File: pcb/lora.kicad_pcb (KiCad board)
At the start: 4 copper layers, 101.9 x 45.1 mm, 91 parts, among them J1 Conn_01x04, J11 Conn_Coaxial, J2 5V, J3 Conn_01x06, J4 USB_C_Receptacle_USB2.0, J5 Temp, J6 VDD, J7 UART, J8 Conn_01x04, Q1 AO3401A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

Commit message: changed a capacity
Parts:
- C3: value 47u -> 10u; footprint Capacitor_SMD:C_1210_3225Metric -> Capacitor_SMD:C_0805_2012Metric
- C4: value 47u -> 22u
- moved R3 3.89 mm to (222.2, 130.3), turned to -90 degrees
- moved SW1 3.56 mm to (225.8, 132.6)
- moved C3 0.62 mm to (185.2, 103.4)
- renumbered Ce to C13
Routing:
- net RESET: track 35.5 -> 31.3 mm
- net GND: track 235.0 -> 230.8 mm
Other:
- outline, holes or cut-outs redrawn
- board text added: "+"
- board text added: "Active"
- board text removed: "Status"

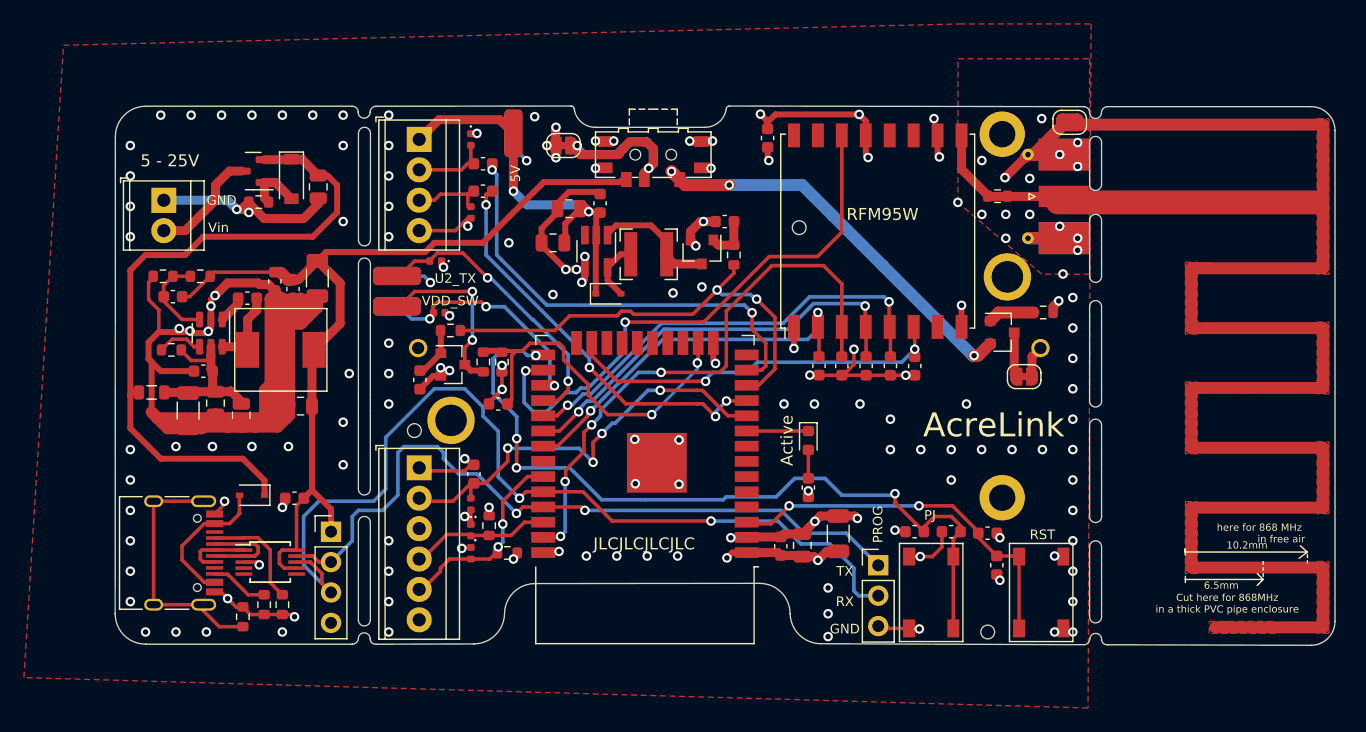
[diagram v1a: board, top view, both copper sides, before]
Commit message: added cutout for cable tie to secure battery
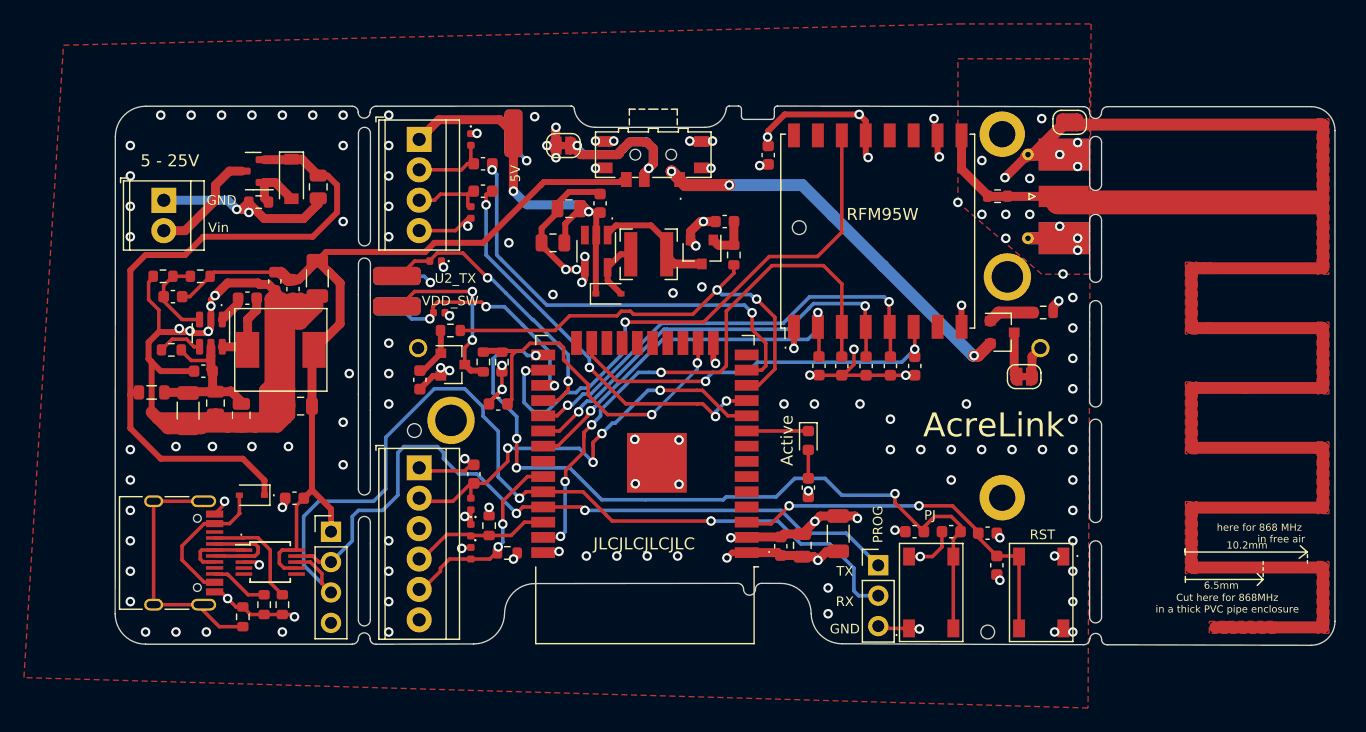
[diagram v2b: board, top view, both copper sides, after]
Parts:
- moved C9 1.43 mm to (203.1, 96.0)
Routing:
- net VDD: track 57.1 -> 56.6 mm
- net GND: track 230.8 -> 230.4 mm, vias 145 -> 144
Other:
- outline, holes or cut-outs redrawn
- board text added: "."

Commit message: updated readme
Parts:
- R1, R11, R13, R17, R2, R20, R23, R24, R3, R4, R5, R6, R9: footprint Capacitor_SMD:C_0603_1608Metric -> Resistor_SMD:R_0603_1608Metric
- moved JP3 1.08 mm to (185.1, 95.8)
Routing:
- net Net-(JP3-Pad1): track 20.6 -> 11.0 mm
- net VDD: track 56.6 -> 55.6 mm
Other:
- board text added: "V_EXT"
- board text removed: "V_EXT/OFF"

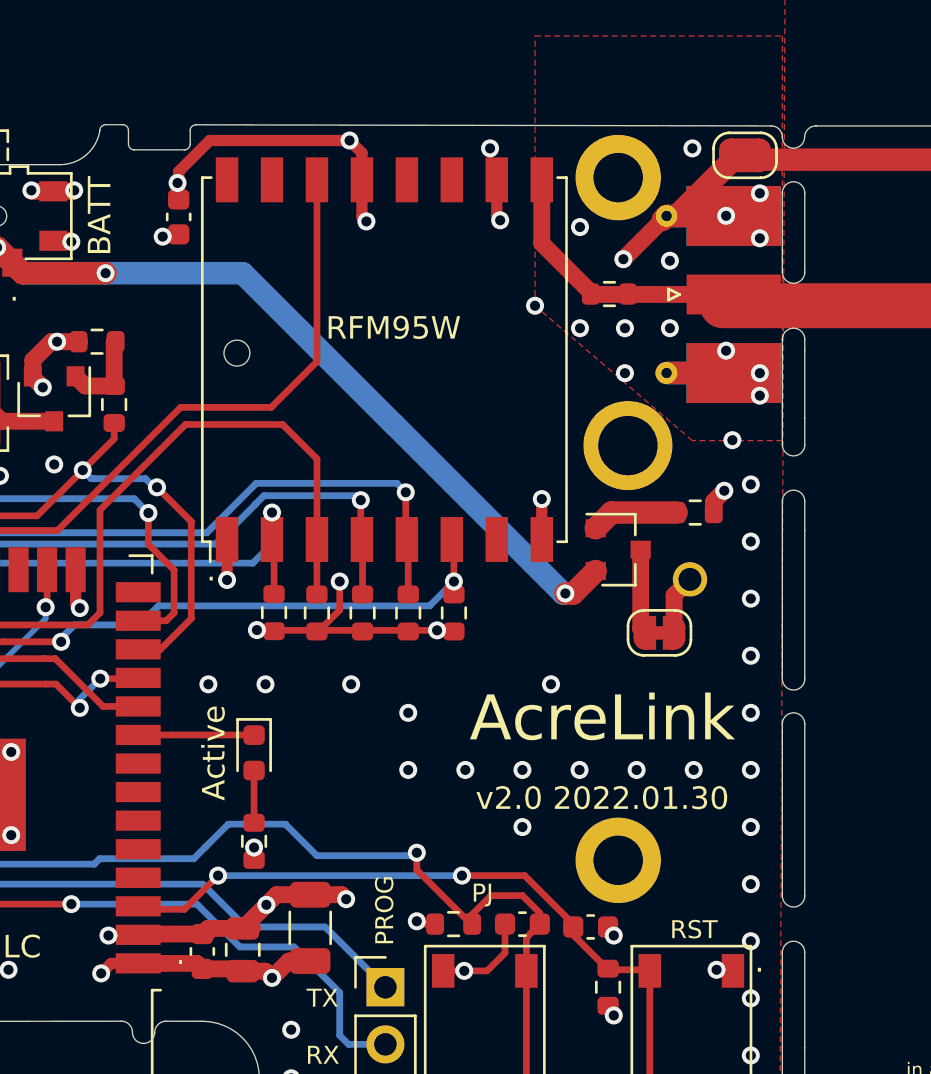
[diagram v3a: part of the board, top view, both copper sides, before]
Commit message: added spi header and connected dio1 of rfm95
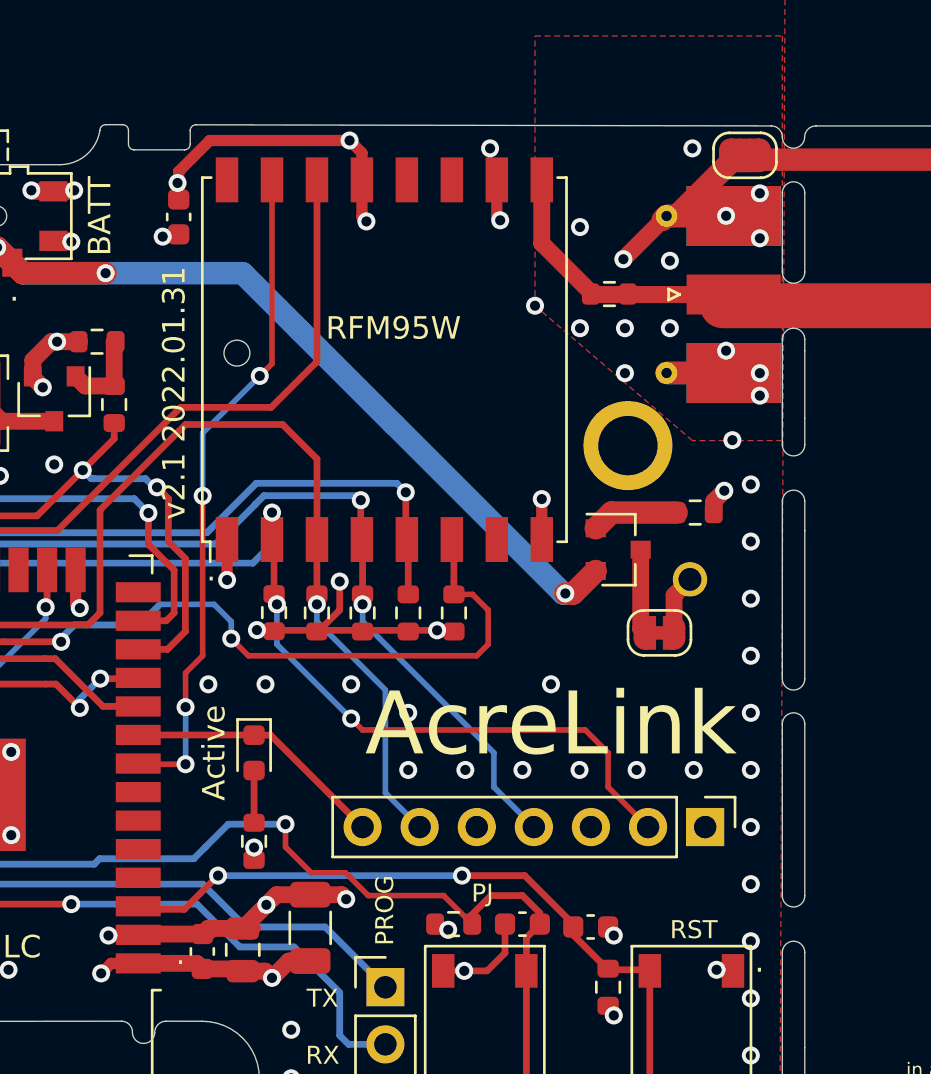
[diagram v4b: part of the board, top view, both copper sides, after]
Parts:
- removed H1, H3: MountingHole_Pad, MountingHole:MountingHole_2.2mm_M2_DIN965_Pad
- added J9: Conn_01x07, Connector_PinHeader_2.54mm:PinHeader_1x07_P2.54mm_Vertical, F.Cu at (226.6, 123.2)
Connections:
- U2 pad 8: unconnected-(U2-Pad8) -> RFM_DIO1
- U4 pad 15: unconnected-(U4-Pad15) -> RFM_DIO1
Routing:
- net RFM_DIO1: track 0.00 -> 29.7 mm, vias 0 -> 4
- net SPI_MISO: track 34.3 -> 57.4 mm, vias 2 -> 4
- net SPI_SCK: track 36.0 -> 49.6 mm, vias 2 -> 3
- net SPI_MOSI: track 48.1 -> 60.4 mm, vias 4 -> 5
- net LED_SIGNAL: track 5.15 -> 11.7 mm
- net RFM_RST: track 33.5 -> 39.5 mm
- net GND: vias 144 -> 143
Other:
- board text added: "3.6V MAX!"
- board text added: "CS"
- board text added: "LifePo4 or Lithium-Thionyl-Chlorid"
- board text added: "MISO"
- board text added: "MOSI"
- board text added: "SCK"
- board text added: "v2.1 2022.01.31"
- board text removed: "LifePo4 or Lithium-Thionyl-Chlorid 3.6V MAX!"
- board text removed: "v2.0 2022.01.30"
